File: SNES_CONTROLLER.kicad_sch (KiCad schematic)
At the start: 24 parts, among them J1 Screw_Terminal_01x06, J2 Screw_Terminal_01x12, J3 Screw_Terminal_01x12, U1 4021, U2 4021

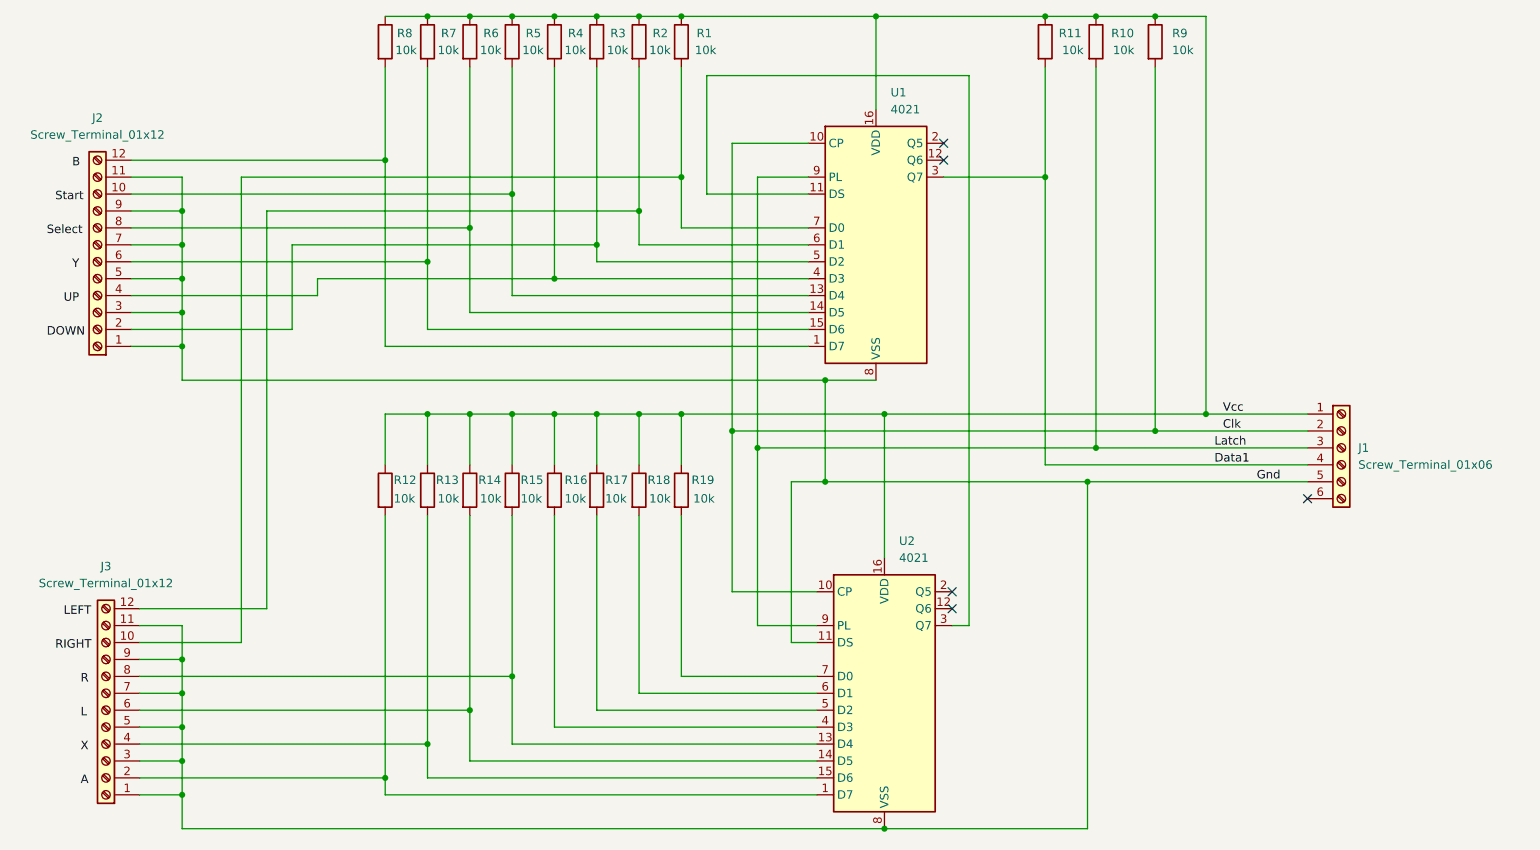
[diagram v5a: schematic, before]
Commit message: Add silkscreens and M4 mount holes
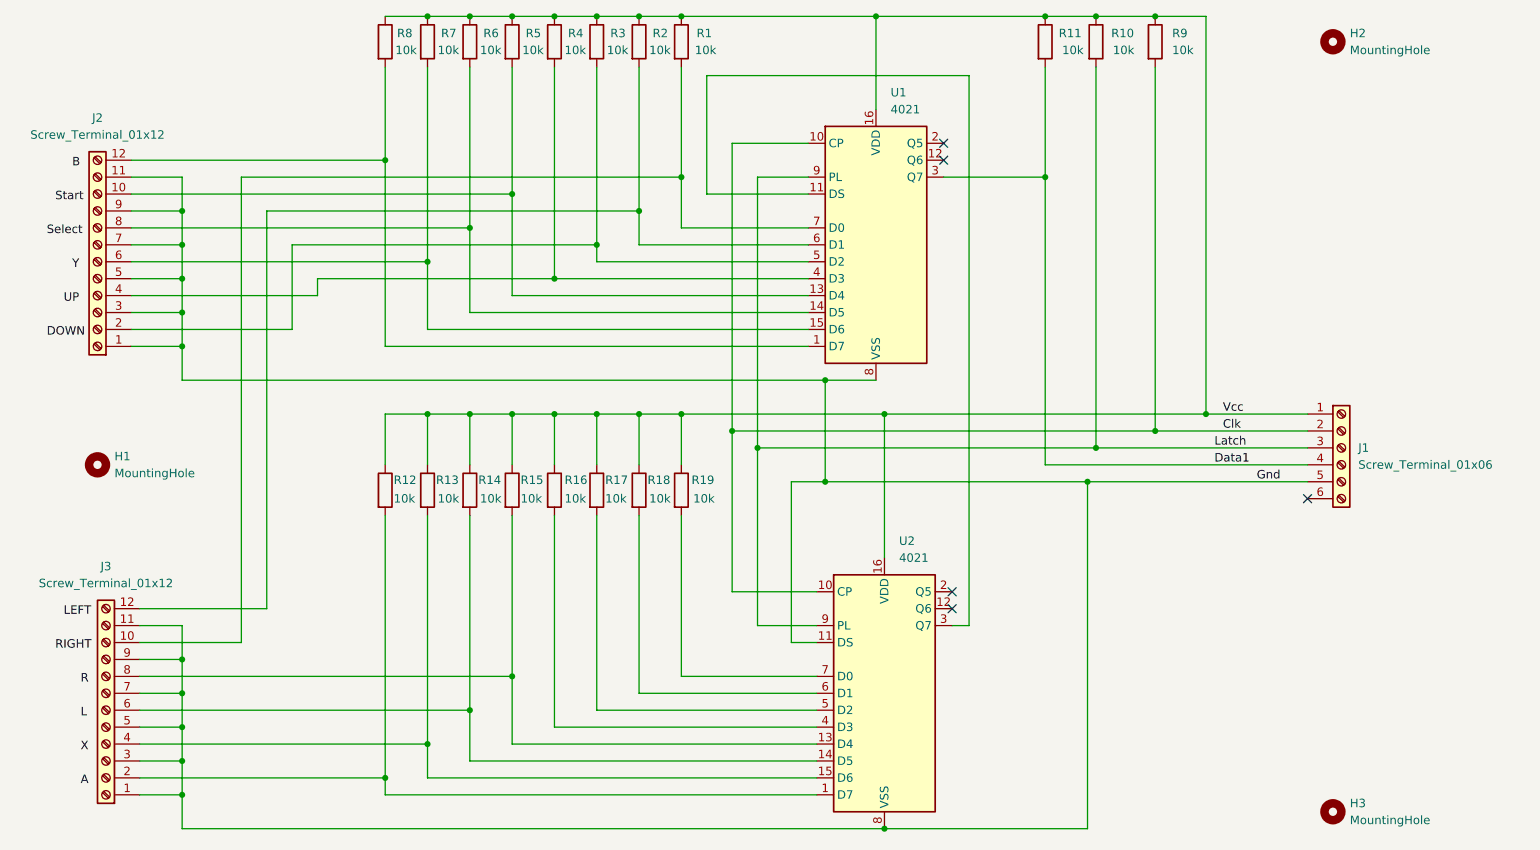
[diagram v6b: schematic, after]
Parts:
- added H1, H2, H3: MountingHole, MountingHole:MountingHole_4.3mm_M4, symbol Mechanical:MountingHole
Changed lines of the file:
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@@
 (kicad_sch
-	(version 20231120)
+	(version 20250114)
 	(generator "eeschema")
-	(generator_version "8.0")
+	(generator_version "9.0")
 	(paper "A4")
 	(junction
@@
 	)
 	(symbol
+		(lib_id "Mechanical:MountingHole")
+		(at 218.44 44.45 0)
+		(unit 1)
+		(exclude_from_sim yes)
+		(in_bom no)
+		(on_board yes)
+		(dnp no)
+		(fields_autoplaced yes)
+		(property "Reference" "H2"
+			(at 220.98 43.1799 0)
+			(effects
+				(font
+					(size 1.27 1.27)
+				)
+				(justify left)
+			)
+		)
+		(property "Value" "MountingHole"
+			(at 220.98 45.7199 0)
+			(effects
+				(font
+					(size 1.27 1.27)
+				)
+				(justify left)
+			)
+		)
+		(property "Footprint" "MountingHole:MountingHole_4.3mm_M4"
+			(at 218.44 44.45 0)
+			(effects
+				(font
+					(size 1.27 1.27)
+				)
+				(hide yes)
+			)
+		)
+		(property "Datasheet" "~"
+			(at 218.44 44.45 0)
+			(effects
+				(font
+					(size 1.27 1.27)
+				)
+				(hide yes)
+			)
+		)
+		(property "Description" "Mounting Hole without connection"
+			(at 218.44 44.45 0)
+			(effects
+				(font
+					(size 1.27 1.27)
+				)
+				(hide yes)
+			)
+		)
+		(instances
+			(project ""
+				(path "/719592b0-85a8-4eb6-8d13-f447981f3475"
+					(reference "H2")
+					(unit 1)
+				)
+			)
+		)
+	)
+	(symbol
 		(lib_id "Device:R")
 		(at 101.6 44.45 0)
@@
 	)
 	(symbol
+		(lib_id "Mechanical:MountingHole")
+		(at 218.44 160.02 0)
+		(unit 1)
+		(exclude_from_sim yes)
+		(in_bom no)
+		(on_board yes)
+		(dnp no)
+		(fields_autoplaced yes)
+		(property "Reference" "H3"
+			(at 220.98 158.7499 0)
+			(effects
+				(font
+					(size 1.27 1.27)
+				)
+				(justify left)
+			)
+		)
+		(property "Value" "MountingHole"
+			(at 220.98 161.2899 0)
+			(effects
+				(font
+					(size 1.27 1.27)
+				)
+				(justify left)
+			)
+		)
+		(property "Footprint" "MountingHole:MountingHole_4.3mm_M4"
+			(at 218.44 160.02 0)
+			(effects
+				(font
+					(size 1.27 1.27)
+				)
+				(hide yes)
+			)
+		)
+		(property "Datasheet" "~"
+			(at 218.44 160.02 0)
+			(effects
+				(font
+					(size 1.27 1.27)
+				)
+				(hide yes)
+			)
+		)
+		(property "Description" "Mounting Hole without connection"
+			(at 218.44 160.02 0)
+			(effects
+				(font
+					(size 1.27 1.27)
+				)
+				(hide yes)
+			)
+		)
+		(instances
+			(project ""
+				(path "/719592b0-85a8-4eb6-8d13-f447981f3475"
+					(reference "H3")
+					(unit 1)
+				)
+			)
+		)
+	)
+	(symbol
 		(lib_id "Device:R")
 		(at 120.65 111.76 0)
@@
 		)
 	)
+	(symbol
+		(lib_id "Mechanical:MountingHole")
+		(at 33.02 107.95 0)
+		(unit 1)
+		(exclude_from_sim yes)
+		(in_bom no)
+		(on_board yes)
+		(dnp no)
+		(fields_autoplaced yes)
+		(property "Reference" "H1"
+			(at 35.56 106.6799 0)
+			(effects
+				(font
+					(size 1.27 1.27)
+				)
+				(justify left)
+			)
+		)
+		(property "Value" "MountingHole"
+			(at 35.56 109.2199 0)
+			(effects
+				(font
+					(size 1.27 1.27)
+				)
+				(justify left)
+			)
+		)
+		(property "Footprint" "MountingHole:MountingHole_4.3mm_M4"
+			(at 33.02 107.95 0)
+			(effects
+				(font
+					(size 1.27 1.27)
+				)
+				(hide yes)
+			)
+		)
+		(property "Datasheet" "~"
+			(at 33.02 107.95 0)
+			(effects
+				(font
+					(size 1.27 1.27)
+				)
+				(hide yes)
+			)
+		)
+		(property "Description" "Mounting Hole without connection"
+			(at 33.02 107.95 0)
+			(effects
+				(font
+					(size 1.27 1.27)
+				)
+				(hide yes)
+			)
+		)
+		(instances
+			(project ""
+				(path "/719592b0-85a8-4eb6-8d13-f447981f3475"
+					(reference "H1")
+					(unit 1)
+				)
+			)
+		)
+	)
 	(sheet_instances
 		(path "/"
@@
 		)
 	)
+	(embedded_fonts no)
 )

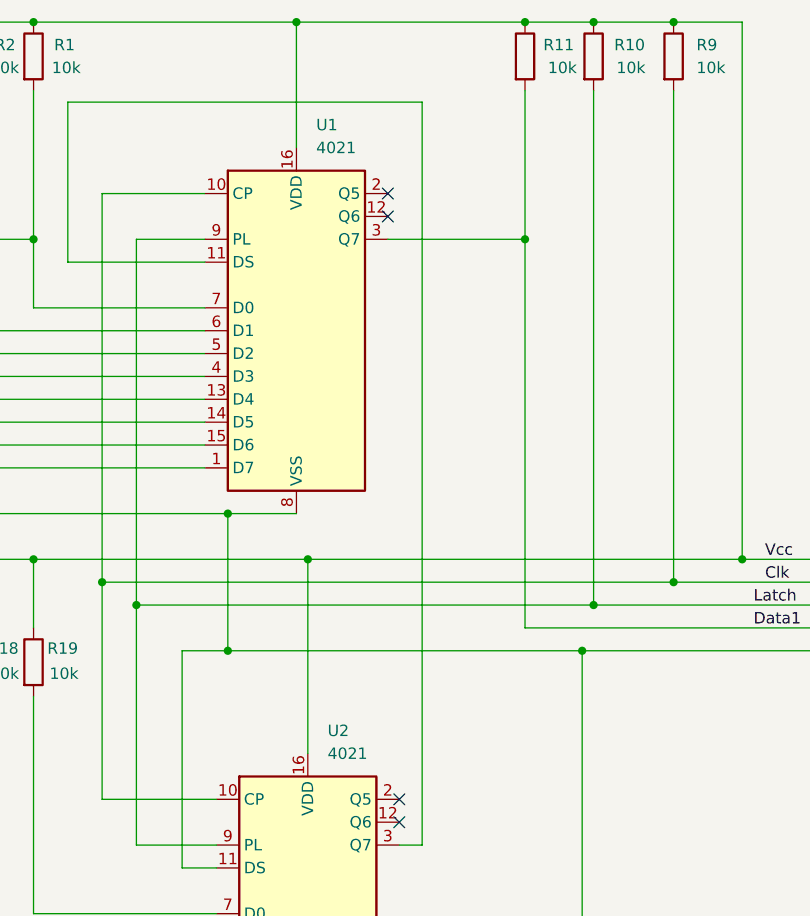
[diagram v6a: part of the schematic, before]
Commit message: Add decoupling capacitors for ICs
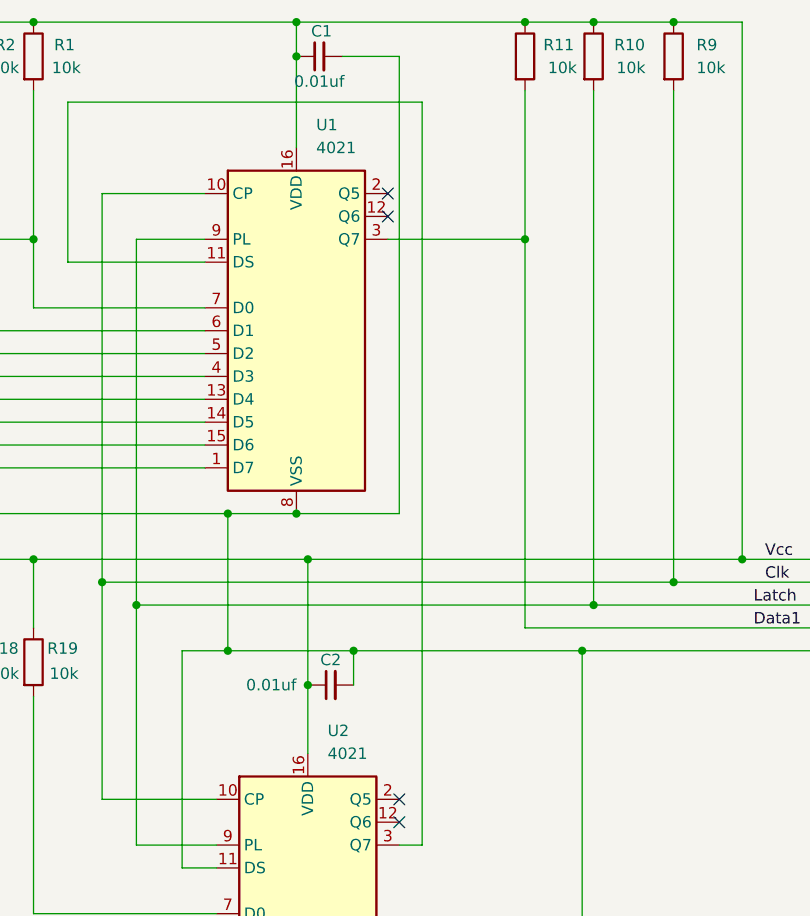
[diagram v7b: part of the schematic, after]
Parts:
- added C1, C2: 0.01uf, Capacitor_THT:C_Disc_D3.0mm_W1.6mm_P2.50mm, symbol Device:C_Small
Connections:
- net Gnd: now also C1.2, C2.2
- net Vcc: now also C1.1, C2.1
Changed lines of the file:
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@@
 	)
 	(junction
+		(at 151.13 114.3)
+		(diameter 0)
+		(color 0 0 0 0)
+	)
+	(junction
 		(at 45.72 69.85)
 		(diameter 0)
@@
 	)
 	(junction
+		(at 149.86 44.45)
+		(diameter 0)
+		(color 0 0 0 0)
+	)
+	(junction
 		(at 191.77 40.64)
 		(diameter 0)
@@
 	)
 	(junction
+		(at 156.21 110.49)
+		(diameter 0)
+		(color 0 0 0 0)
+	)
+	(junction
 		(at 82.55 77.47)
 		(diameter 0)
@@
 	)
 	(junction
+		(at 149.86 95.25)
+		(diameter 0)
+		(color 0 0 0 0)
+	)
+	(junction
 		(at 82.55 100.33)
 		(diameter 0)
@@
 	(wire
 		(pts
+			(xy 156.21 110.49) (xy 156.21 114.3)
+		)
+		(stroke
+			(width 0)
+			(type default)
+		)
+	)
+	(wire
+		(pts
 			(xy 38.1 62.23) (xy 76.2 62.23)
 		)
@@
 	(wire
 		(pts
+			(xy 156.21 110.49) (xy 181.61 110.49)
+		)
+		(stroke
+			(width 0)
+			(type default)
+		)
+	)
+	(wire
+		(pts
 			(xy 182.88 105.41) (xy 214.63 105.41)
 		)
@@
 	(wire
 		(pts
+			(xy 151.13 114.3) (xy 151.13 100.33)
+		)
+		(stroke
+			(width 0)
+			(type default)
+		)
+	)
+	(wire
+		(pts
 			(xy 45.72 80.01) (xy 45.72 74.93)
 		)
@@
 	(wire
 		(pts
+			(xy 161.29 95.25) (xy 149.86 95.25)
+		)
+		(stroke
+			(width 0)
+			(type default)
+		)
+	)
+	(wire
+		(pts
 			(xy 62.23 74.93) (xy 107.95 74.93)
 		)
@@
 	(wire
 		(pts
+			(xy 154.94 44.45) (xy 161.29 44.45)
+		)
+		(stroke
+			(width 0)
+			(type default)
+		)
+	)
+	(wire
+		(pts
 			(xy 107.95 48.26) (xy 107.95 74.93)
 		)
@@
 	(wire
 		(pts
-			(xy 151.13 121.92) (xy 151.13 100.33)
+			(xy 151.13 121.92) (xy 151.13 114.3)
 		)
 		(stroke
@@
 	(wire
 		(pts
+			(xy 161.29 44.45) (xy 161.29 95.25)
+		)
+		(stroke
+			(width 0)
+			(type default)
+		)
+	)
+	(wire
+		(pts
 			(xy 66.04 82.55) (xy 66.04 80.01)
 		)
@@
 	(wire
 		(pts
-			(xy 149.86 40.64) (xy 149.86 54.61)
+			(xy 149.86 40.64) (xy 149.86 44.45)
 		)
 		(stroke
@@
 	(wire
 		(pts
-			(xy 142.24 110.49) (xy 181.61 110.49)
+			(xy 142.24 110.49) (xy 156.21 110.49)
 		)
 		(stroke
@@
 	(wire
 		(pts
+			(xy 149.86 44.45) (xy 149.86 54.61)
+		)
+		(stroke
+			(width 0)
+			(type default)
+		)
+	)
+	(wire
+		(pts
 			(xy 120.65 72.39) (xy 139.7 72.39)
 		)
@@
 	)
 	(symbol
+		(lib_id "Device:C_Small")
+		(at 152.4 44.45 90)
+		(unit 1)
+		(exclude_from_sim no)
+		(in_bom yes)
+		(on_board yes)
+		(dnp no)
+		(property "Reference" "C1"
+			(at 152.654 41.656 90)
+			(effects
+				(font
+					(size 1.27 1.27)
+				)
+			)
+		)
+		(property "Value" "0.01uf"
+			(at 152.4 47.244 90)
+			(effects
+				(font
+					(size 1.27 1.27)
+				)
+			)
+		)
+		(property "Footprint" "Capacitor_THT:C_Disc_D3.0mm_W1.6mm_P2.50mm"
+			(at 152.4 44.45 0)
+			(effects
+				(font
+					(size 1.27 1.27)
+				)
+				(hide yes)
+			)
+		)
+		(property "Datasheet" "~"
+			(at 152.4 44.45 0)
+			(effects
+				(font
+					(size 1.27 1.27)
+				)
+				(hide yes)
+			)
+		)
+		(property "Description" "Unpolarized capacitor, small symbol"
+			(at 152.4 44.45 0)
+			(effects
+				(font
+					(size 1.27 1.27)
+				)
+				(hide yes)
+			)
+		)
+		(pin "1"
+		)
+		(pin "2"
+		)
+		(instances
+			(project ""
+				(path "/719592b0-85a8-4eb6-8d13-f447981f3475"
+					(reference "C1")
+					(unit 1)
+				)
+			)
+		)
+	)
+	(symbol
 		(lib_id "Device:R")
 		(at 88.9 111.76 0)
@@
 					(unit 1)
 				)
+			)
+		)
+	)
+	(symbol
+		(lib_id "Device:C_Small")
+		(at 153.67 114.3 90)
+		(unit 1)
+		(exclude_from_sim no)
+		(in_bom yes)
+		(on_board yes)
+		(dnp no)
+		(property "Reference" "C2"
+			(at 153.67 111.506 90)
+			(effects
+				(font
+					(size 1.27 1.27)
+				)
+			)
+		)
+		(property "Value" "0.01uf"
+			(at 147.066 114.3 90)
+			(effects
+				(font
+					(size 1.27 1.27)
+				)
+			)
+		)
+		(property "Footprint" "Capacitor_THT:C_Disc_D3.0mm_W1.6mm_P2.50mm"
+			(at 153.67 114.3 0)
+			(effects
+				(font
+					(size 1.27 1.27)
+				)
+				(hide yes)
+			)
+		)
+		(property "Datasheet" "~"
+			(at 153.67 114.3 0)
+			(effects
+				(font
+					(size 1.27 1.27)
+				)
+				(hide yes)
+			)
+		)
+		(property "Description" "Unpolarized capacitor, small symbol"
+			(at 153.67 114.3 0)
+			(effects
+				(font
+					(size 1.27 1.27)
+				)
+				(hide yes)
+			)
+		)
+		(pin "2"
+		)
+		(pin "1"
+		)
+		(instances
+			(project ""
+				(path "/719592b0-85a8-4eb6-8d13-f447981f3475"
+					(reference "C2")
+					(unit 1)
+				)

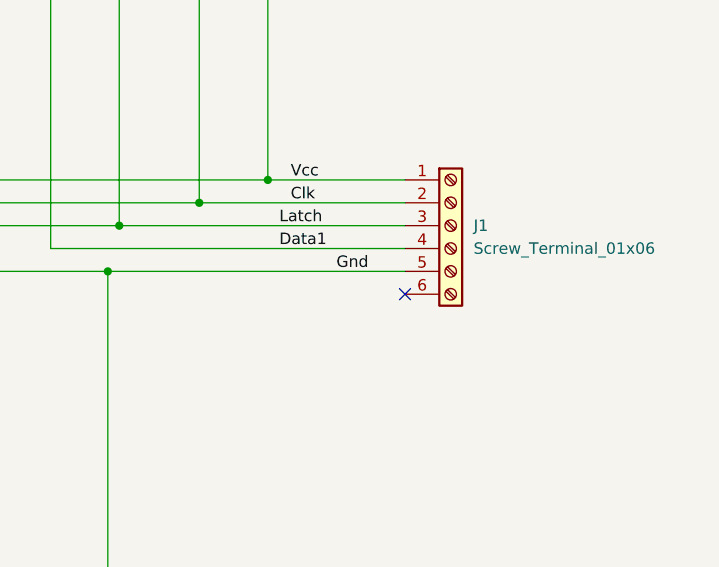
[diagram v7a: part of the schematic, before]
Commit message: Refactor schematic and board
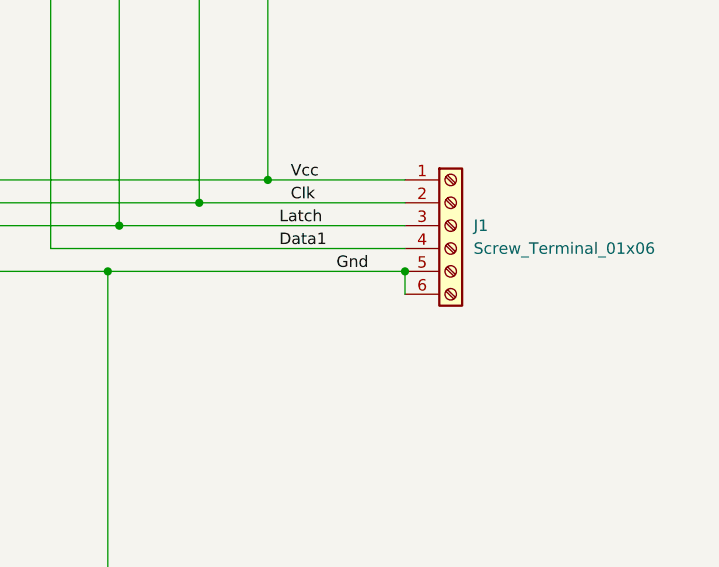
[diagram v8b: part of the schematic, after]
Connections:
- net Gnd: now also J1.6 (Pin_6)
- no-connect marks 5 -> 4
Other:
- title: (none) -> SNES & Uzebox Modular Joystick PCB
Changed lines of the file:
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@@
 	(generator_version "9.0")
 	(paper "A4")
+	(title_block
+		(title "SNES & Uzebox Modular Joystick PCB")
+		(date "2025-05-06")
+		(rev "1.5")
+	)
 	(junction
 		(at 88.9 72.39)
@@
 	(junction
 		(at 45.72 90.17)
+		(diameter 0)
+		(color 0 0 0 0)
+	)
+	(junction
+		(at 214.63 110.49)
 		(diameter 0)
 		(color 0 0 0 0)
@@
 	)
 	(no_connect
-		(at 214.63 113.03)
-	)
-	(no_connect
 		(at 161.29 127)
 	)
@@
 		)
 		(stroke
+			(width 0)
+			(type default)
+		)
+	)
+	(wire
+		(pts
+			(xy 214.63 110.49) (xy 214.63 113.03)
+		)
+		(stroke
